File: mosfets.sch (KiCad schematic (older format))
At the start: 79 parts, among them P5 HP_MOSFETS, P6 MP_MOSFETS, Q1 2N7002P, Q10 2N7002P, Q11 2N7002P, Q12 BC846BPDW1, Q13 BC846BPDW1, Q14 SI2318CDS-T1-GE3, Q15 IRFB7545PbF, Q16 2N7002P, Q17 2N7002P, Q18 BC846BPDW1, Q19 BC846BPDW1, Q2 2N7002P, Q20 SI2318CDS-T1-GE3, Q21 IRFB7545PbF, Q3 2N7002P, Q4 BC846BPDW1, Q5 BC846BPDW1, Q6 BC846BPDW1, Q7 IRFB7545PbF, Q8 SI2318CDS-T1-GE3, Q9 IRFB7545PbF

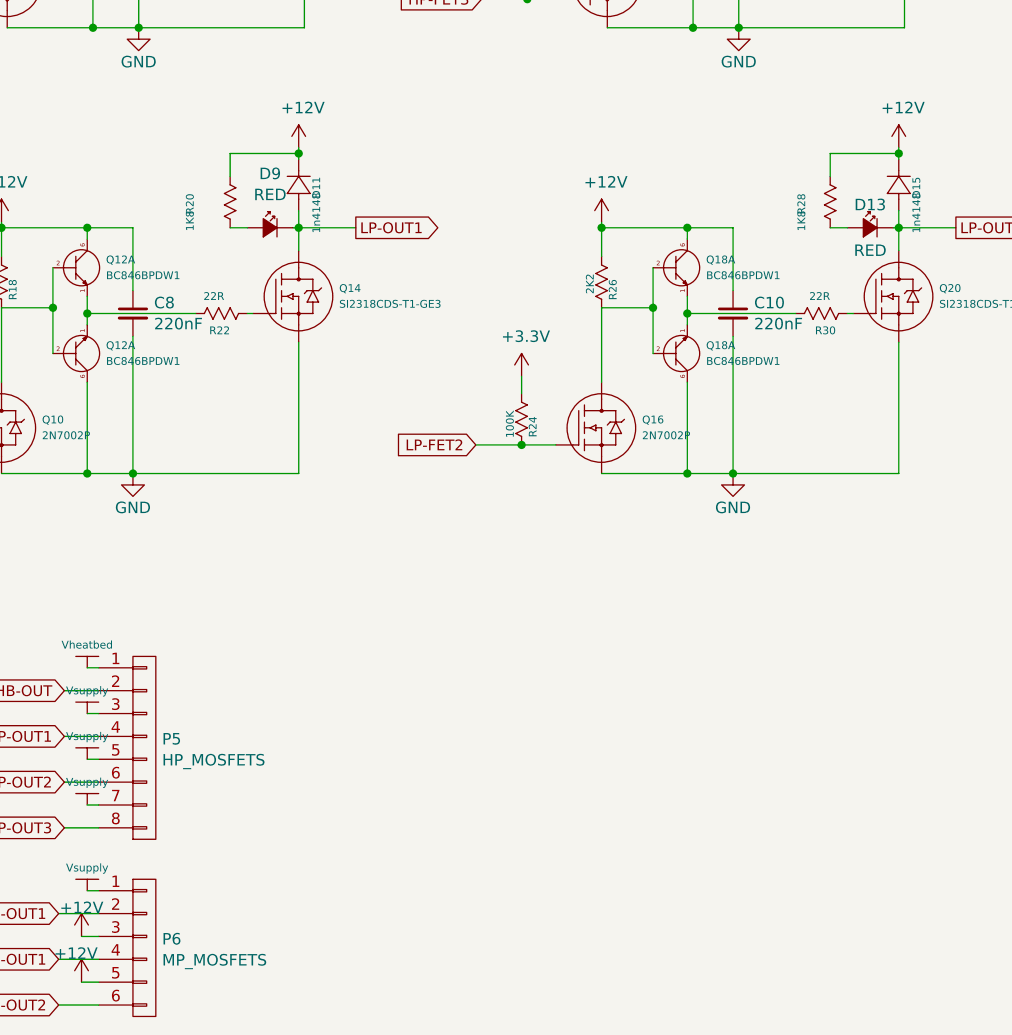
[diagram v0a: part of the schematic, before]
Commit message: Added specifications and manufacturers to component attributes
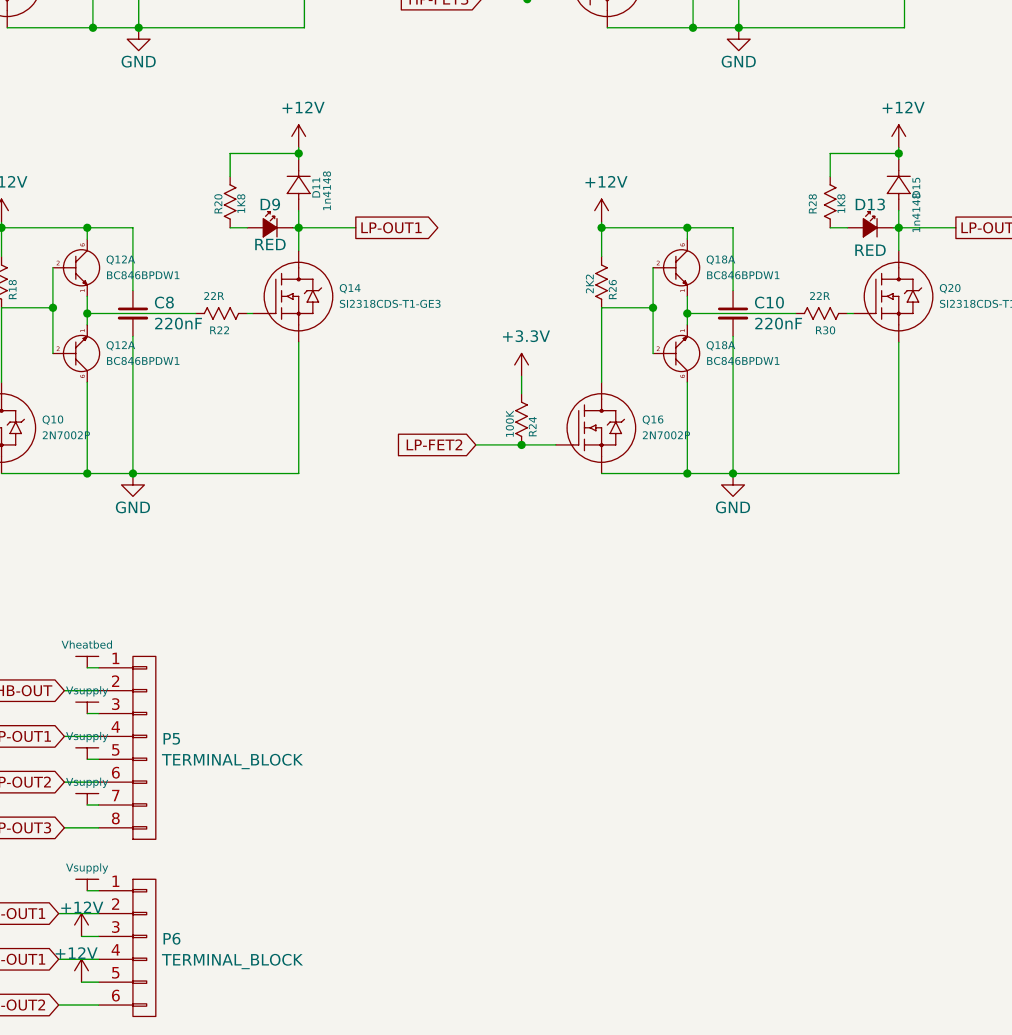
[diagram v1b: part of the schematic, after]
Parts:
- D10, D13, D14, D3, D4, D5, D9: Manufacturer (none) -> Lite-On; ManufacturerNo (none) -> LTST-C193KRKT-5A
- D11, D15, D7: Manufacturer (none) -> Fairchild Semiconductor; ManufacturerNo (none) -> FDLL4148
- P5: value HP_MOSFETS -> TERMINAL_BLOCK; Comment (none) -> HP_MOSFETS; Manufacturer (none) -> Multicomp; ManufacturerNo (none) -> MC000031
- P6: value MP_MOSFETS -> TERMINAL_BLOCK; Comment (none) -> MP_MOSFETS; Manufacturer (none) -> Multicomp; ManufacturerNo (none) -> MC000030
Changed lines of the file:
@@
 F 2 "diodes:LED-0603" H 3000 1200 50  0001 C CNN
 F 3 "" H 3000 1200 50  0000 C CNN
+F 4 "LTST-C193KRKT-5A" H 3000 1200 135 0001 L CNN "ManufacturerNo"
+F 5 "Lite-On" H 3000 1200 135 0001 L CNN "Manufacturer"
 	1    3000 1200
 	-1   0    0    -1
@@
 F 2 "diodes:LED-0603" H 8375 1200 50  0001 C CNN
 F 3 "" H 8375 1200 50  0000 C CNN
+F 4 "LTST-C193KRKT-5A" H 8375 1200 135 0001 L CNN "ManufacturerNo"
+F 5 "Lite-On" H 8375 1200 135 0001 L CNN "Manufacturer"
 	1    8375 1200
 	-1   0    0    -1
@@
 F 2 "diodes:LED-0603" H 2950 5100 50  0001 C CNN
 F 3 "" H 2950 5100 50  0000 C CNN
+F 4 "Lite-On" H 2950 5100 135 0001 L CNN "Manufacturer"
+F 5 "LTST-C193KRKT-5A" H 2950 5100 135 0001 L CNN "ManufacturerNo"
 	1    2950 5100
 	-1   0    0    -1
@@
 F 2 "diodes:LED-0603" H 2975 3150 50  0001 C CNN
 F 3 "" H 2975 3150 50  0000 C CNN
+F 4 "LTST-C193KRKT-5A" H 2975 3150 135 0001 L CNN "ManufacturerNo"
+F 5 "Lite-On" H 2975 3150 135 0001 L CNN "Manufacturer"
 	1    2975 3150
 	-1   0    0    -1
@@
 U 1 1 568B7A4E
 P 5475 2925
-F 0 "R20" H 5550 2825 34  0000 L CNN
-F 1 "1K8" H 5625 2825 34  0000 L CNN
+F 0 "R20" H 5550 2950 34  0000 L CNN
+F 1 "1K8" H 5550 3050 34  0000 L CNN
 F 2 "resistors:R_0603" H 5475 2925 60  0001 C CNN
 F 3 "" H 5475 2925 60  0000 C CNN
@@
 U 1 1 568B7A5F
 P 5725 3150
-F 0 "D9" H 5725 3386 50  0000 C CNN
-F 1 "RED" H 5725 3294 50  0000 C CNN
+F 0 "D9" H 5725 3250 50  0000 C CNN
+F 1 "RED" H 5725 3075 50  0000 C CNN
 F 2 "diodes:LED-0603" H 5725 3150 50  0001 C CNN
 F 3 "" H 5725 3150 50  0000 C CNN
+F 4 "LTST-C193KRKT-5A" H 5725 3150 135 0001 L CNN "ManufacturerNo"
+F 5 "Lite-On" H 5725 3150 135 0001 L CNN "Manufacturer"
 	1    5725 3150
 	-1   0    0    -1
@@
 U 1 1 568B7AC1
 P 8100 2925
-F 0 "R28" H 8175 2875 34  0000 L CNN
-F 1 "1K8" H 8250 2875 34  0000 L CNN
+F 0 "R28" H 8175 2925 34  0000 L CNN
+F 1 "1K8" H 8175 3050 34  0000 L CNN
 F 2 "resistors:R_0603" H 8100 2925 60  0001 C CNN
 F 3 "" H 8100 2925 60  0000 C CNN
@@
 F 2 "diodes:DO213AA_SOD-80_MiniMelf" H 3150 3075 60  0001 C CNN
 F 3 "" H 3150 3075 60  0000 C CNN
+F 4 "Fairchild Semiconductor" H 3150 3075 135 0001 L CNN "Manufacturer"
+F 5 "FDLL4148" H 3150 3075 135 0001 L CNN "ManufacturerNo"
 	1    3150 3075
 	0    -1   -1   0
@@
 P 5900 3075
 F 0 "D11" H 6048 3047 34  0000 R CNN
-F 1 "1n4148" H 5979 3047 34  0000 R CNN
+F 1 "1n4148" H 6075 3000 34  0000 R CNN
 F 2 "diodes:DO213AA_SOD-80_MiniMelf" H 5900 3075 60  0001 C CNN
 F 3 "" H 5900 3075 60  0000 C CNN
+F 4 "FDLL4148" H 5900 3075 135 0001 L CNN "ManufacturerNo"
+F 5 "Fairchild Semiconductor" H 5900 3075 135 0001 L CNN "Manufacturer"
 	1    5900 3075
 	0    -1   -1   0
@@
 F 2 "diodes:DO213AA_SOD-80_MiniMelf" H 8525 3075 60  0001 C CNN
 F 3 "" H 8525 3075 60  0000 C CNN
+F 4 "FDLL4148" H 8525 3075 135 0001 L CNN "ManufacturerNo"
+F 5 "Fairchild Semiconductor" H 8525 3075 135 0001 L CNN "Manufacturer"
 	1    8525 3075
 	0    -1   -1   0
@@
 P 5175 6300
 F 0 "P6" H 5252 6338 50  0000 L CNN
-F 1 "MP_MOSFETS" H 5252 6246 50  0000 L CNN
+F 1 "TERMINAL_BLOCK" H 5252 6246 50  0000 L CNN
 F 2 "terminal_blocks:TERMINAL_BLOCK_6_PIN_5mm" H 5175 6300 50  0001 C CNN
 F 3 "" H 5175 6300 50  0000 C CNN
+F 4 "Multicomp" H 5175 6300 135 0001 L CNN "Manufacturer"
+F 5 "MC000030" H 5175 6300 135 0001 L CNN "ManufacturerNo"
+F 6 "MP_MOSFETS" H 5175 6300 135 0001 L CNN "Comment"
 	1    5175 6300
 	1    0    0    -1
@@
 P 5175 5425
 F 0 "P5" H 5252 5463 50  0000 L CNN
-F 1 "HP_MOSFETS" H 5252 5371 50  0000 L CNN
+F 1 "TERMINAL_BLOCK" H 5252 5371 50  0000 L CNN
 F 2 "terminal_blocks:TERMINAL_BLOCK_8_PIN_5mm" H 5175 5425 50  0001 C CNN
 F 3 "" H 5175 5425 50  0000 C CNN
+F 4 "Multicomp" H 5175 5425 135 0001 L CNN "Manufacturer"
+F 5 "MC000031" H 5175 5425 135 0001 L CNN "ManufacturerNo"
+F 6 "HP_MOSFETS" H 5175 5425 135 0001 L CNN "Comment"
 	1    5175 5425
 	1    0    0    -1
@@
 F 2 "diodes:LED-0603" H 5750 1200 50  0001 C CNN
 F 3 "" H 5750 1200 50  0000 C CNN
+F 4 "LTST-C193KRKT-5A" H 5750 1200 135 0001 L CNN "ManufacturerNo"
+F 5 "Lite-On" H 5750 1200 135 0001 L CNN "Manufacturer"
 	1    5750 1200
 	-1   0    0    -1
@@
 F 2 "diodes:LED-0603" H 8350 3150 50  0001 C CNN
 F 3 "" H 8350 3150 50  0000 C CNN
+F 4 "LTST-C193KRKT-5A" H 8350 3150 135 0001 L CNN "ManufacturerNo"
+F 5 "Lite-On" H 8350 3150 135 0001 L CNN "Manufacturer"
 	1    8350 3150
 	-1   0    0    -1
